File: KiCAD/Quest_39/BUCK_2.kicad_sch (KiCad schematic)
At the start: 33 parts, among them U12 AD626ANZ, U13 INA226, U14 LTM4611EV-PBF, U15 MCP4151-502E/SN

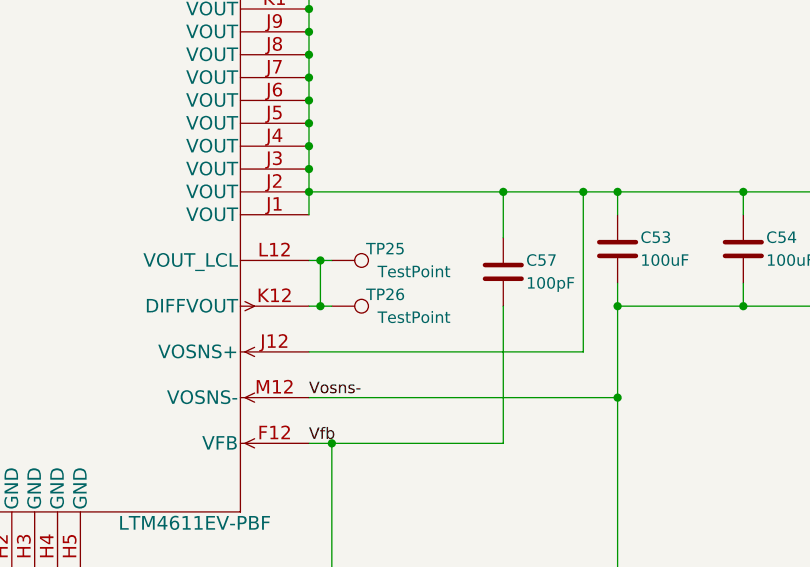
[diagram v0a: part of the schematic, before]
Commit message: Added 3rd buck converter section
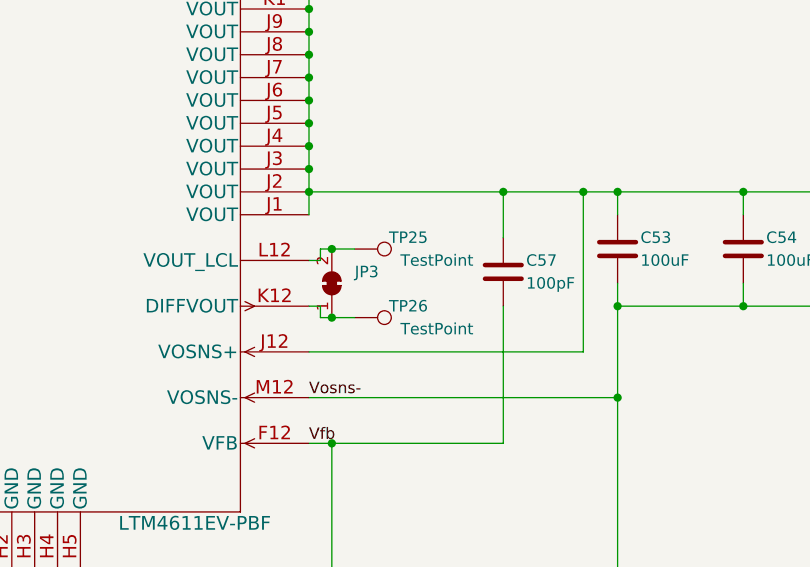
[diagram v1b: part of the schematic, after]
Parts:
- added JP3: SolderJumper_2_Bridged, Jumper:SolderJumper-2_P1.3mm_Bridged_RoundedPad1.0x1.5mm, symbol Jumper:SolderJumper_2_Bridged
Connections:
- net at TP25.1, U14.L12 (VOUT_LCL): now also JP3.2 (B); no longer TP26.1, U14.K12 (DIFFVOUT)
- new net: JP3.1 (A), TP26.1, U14.K12 (DIFFVOUT)
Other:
- moved on the sheet: TP25, TP26
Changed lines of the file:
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@@
   (junction (at 210.82 34.29) (diameter 0) (color 0 0 0 0)
   )
+  (junction (at 325.12 170.18) (diameter 0) (color 0 0 0 0)
+  )
   (junction (at 322.58 148.59) (diameter 0) (color 0 0 0 0)
   )
@@
   (junction (at 198.12 34.29) (diameter 0) (color 0 0 0 0)
   )
+  (junction (at 325.12 162.56) (diameter 0) (color 0 0 0 0)
+  )
   (junction (at 322.58 105.41) (diameter 0) (color 0 0 0 0)
   )
@@
   (junction (at 370.84 156.21) (diameter 0) (color 0 0 0 0)
   )
-  (junction (at 323.85 168.91) (diameter 0) (color 0 0 0 0)
-  )
   (junction (at 203.2 34.29) (diameter 0) (color 0 0 0 0)
   )
@@
   )
   (junction (at 370.84 168.91) (diameter 0) (color 0 0 0 0)
-  )
-  (junction (at 323.85 163.83) (diameter 0) (color 0 0 0 0)
   )
   (junction (at 91.44 34.29) (diameter 0) (color 0 0 0 0)
@@
     (stroke (width 0) (type default) (color 0 0 0 0))
   )
-  (wire (pts (xy 325.12 168.91) (xy 323.85 168.91))
-    (stroke (width 0) (type default) (color 0 0 0 0))
-  )
   (wire (pts (xy 322.58 140.97) (xy 322.58 143.51))
     (stroke (width 0) (type default) (color 0 0 0 0))
@@
     (stroke (width 0) (type default) (color 0 0 0 0))
   )
-  (wire (pts (xy 323.85 168.91) (xy 322.58 168.91))
-    (stroke (width 0) (type default) (color 0 0 0 0))
-  )
   (wire (pts (xy 322.58 62.23) (xy 322.58 64.77))
     (stroke (width 0) (type default) (color 0 0 0 0))
@@
     (stroke (width 0) (type default) (color 0 0 0 0))
   )
+  (wire (pts (xy 325.12 170.18) (xy 327.66 170.18))
+    (stroke (width 0) (type default) (color 0 0 0 0))
+  )
   (wire (pts (xy 208.28 34.29) (xy 210.82 34.29))
     (stroke (width 0) (type default) (color 0 0 0 0))
@@
     (stroke (width 0) (type default) (color 0 0 0 0))
   )
+  (wire (pts (xy 322.58 163.83) (xy 323.85 163.83))
+    (stroke (width 0) (type default) (color 0 0 0 0))
+  )
   (polyline (pts (xy 351.79 203.2) (xy 351.79 233.68))
     (stroke (width 0) (type default) (color 0 0 0 0))
@@
     (stroke (width 0) (type default) (color 0 0 0 0))
   )
-  (wire (pts (xy 323.85 163.83) (xy 323.85 168.91))
-    (stroke (width 0) (type default) (color 0 0 0 0))
-  )
   (wire (pts (xy 322.58 69.85) (xy 322.58 72.39))
     (stroke (width 0) (type default) (color 0 0 0 0))
@@
     (stroke (width 0) (type default) (color 0 0 0 0))
   )
+  (wire (pts (xy 322.58 168.91) (xy 323.85 168.91))
+    (stroke (width 0) (type default) (color 0 0 0 0))
+  )
   (wire (pts (xy 91.44 34.29) (xy 105.41 34.29))
     (stroke (width 0) (type default) (color 0 0 0 0))
@@
     (stroke (width 0) (type default) (color 0 0 0 0))
   )
+  (wire (pts (xy 323.85 170.18) (xy 325.12 170.18))
+    (stroke (width 0) (type default) (color 0 0 0 0))
+  )
   (wire (pts (xy 20.32 63.5) (xy 25.4 63.5))
     (stroke (width 0) (type default) (color 0 0 0 0))
@@
     (stroke (width 0) (type default) (color 0 0 0 0))
   )
+  (wire (pts (xy 325.12 162.56) (xy 327.66 162.56))
+    (stroke (width 0) (type default) (color 0 0 0 0))
+  )
   (wire (pts (xy 95.25 115.57) (xy 105.41 115.57))
     (stroke (width 0) (type default) (color 0 0 0 0))
@@
     (stroke (width 0) (type default) (color 0 0 0 0))
   )
-  (wire (pts (xy 323.85 163.83) (xy 325.12 163.83))
-    (stroke (width 0) (type default) (color 0 0 0 0))
-  )
   (wire (pts (xy 175.26 34.29) (xy 177.8 34.29))
     (stroke (width 0) (type default) (color 0 0 0 0))
@@
     (stroke (width 0) (type default) (color 0 0 0 0))
   )
-  (wire (pts (xy 322.58 163.83) (xy 323.85 163.83))
-    (stroke (width 0) (type default) (color 0 0 0 0))
-  )
   (wire (pts (xy 198.12 34.29) (xy 198.12 39.37))
     (stroke (width 0) (type default) (color 0 0 0 0))
@@
     (stroke (width 0) (type default) (color 0 0 0 0))
   )
+  (wire (pts (xy 323.85 163.83) (xy 323.85 162.56))
+    (stroke (width 0) (type default) (color 0 0 0 0))
+  )
   (polyline (pts (xy 13.97 26.67) (xy 87.63 26.67))
     (stroke (width 0) (type default) (color 0 0 0 0))
@@
     (stroke (width 0) (type default) (color 0 0 0 0))
   )
+  (wire (pts (xy 323.85 162.56) (xy 325.12 162.56))
+    (stroke (width 0) (type default) (color 0 0 0 0))
+  )
   (wire (pts (xy 370.84 156.21) (xy 370.84 158.75))
+    (stroke (width 0) (type default) (color 0 0 0 0))
+  )
+  (wire (pts (xy 323.85 168.91) (xy 323.85 170.18))
     (stroke (width 0) (type default) (color 0 0 0 0))
   )
@@
     (pin "2")
   )
-  (symbol (lib_id "Connector:TestPoint") (at 325.12 163.83 270) (unit 1)
-    (in_bom yes) (on_board yes)
-    (property "Reference" "TP25" (id 0) (at 328.93 162.56 90)
-      (effects (font (size 1.27 1.27)) (justify left))
-    )
-    (property "Value" "TestPoint" (id 1) (at 330.2 165.1 90)
-      (effects (font (size 1.27 1.27)) (justify left))
-    )
-    (property "Footprint" "TestPoint:TestPoint_Pad_D2.0mm" (id 2) (at 325.12 168.91 0)
-      (effects (font (size 1.27 1.27)) hide)
-    )
-    (property "Datasheet" "~" (id 3) (at 325.12 168.91 0)
+  (symbol (lib_id "Connector:TestPoint") (at 327.66 162.56 270) (unit 1)
+    (in_bom yes) (on_board yes)
+    (property "Reference" "TP25" (id 0) (at 331.47 161.29 90)
+      (effects (font (size 1.27 1.27)) (justify left))
+    )
+    (property "Value" "TestPoint" (id 1) (at 332.74 163.83 90)
+      (effects (font (size 1.27 1.27)) (justify left))
+    )
+    (property "Footprint" "TestPoint:TestPoint_Pad_D2.0mm" (id 2) (at 327.66 167.64 0)
+      (effects (font (size 1.27 1.27)) hide)
+    )
+    (property "Datasheet" "~" (id 3) (at 327.66 167.64 0)
       (effects (font (size 1.27 1.27)) hide)
     )
@@
     (pin "2")
   )
-  (symbol (lib_id "Connector:TestPoint") (at 325.12 168.91 270) (unit 1)
-    (in_bom yes) (on_board yes)
-    (property "Reference" "TP26" (id 0) (at 328.93 167.64 90)
-      (effects (font (size 1.27 1.27)) (justify left))
-    )
-    (property "Value" "TestPoint" (id 1) (at 330.2 170.18 90)
-      (effects (font (size 1.27 1.27)) (justify left))
-    )
-    (property "Footprint" "TestPoint:TestPoint_Pad_D2.0mm" (id 2) (at 325.12 173.99 0)
-      (effects (font (size 1.27 1.27)) hide)
-    )
-    (property "Datasheet" "~" (id 3) (at 325.12 173.99 0)
+  (symbol (lib_id "Connector:TestPoint") (at 327.66 170.18 270) (unit 1)
+    (in_bom yes) (on_board yes)
+    (property "Reference" "TP26" (id 0) (at 331.47 168.91 90)
+      (effects (font (size 1.27 1.27)) (justify left))
+    )
+    (property "Value" "TestPoint" (id 1) (at 332.74 171.45 90)
+      (effects (font (size 1.27 1.27)) (justify left))
+    )
+    (property "Footprint" "TestPoint:TestPoint_Pad_D2.0mm" (id 2) (at 327.66 175.26 0)
+      (effects (font (size 1.27 1.27)) hide)
+    )
+    (property "Datasheet" "~" (id 3) (at 327.66 175.26 0)
       (effects (font (size 1.27 1.27)) hide)
     )
@@
       (effects (font (size 1.27 1.27)) hide)
     )
+    (pin "1")
+    (pin "2")
+  )
+  (symbol (lib_id "Jumper:SolderJumper_2_Bridged") (at 325.12 166.37 90) (unit 1)
+    (in_bom yes) (on_board yes) (fields_autoplaced)
+    (property "Reference" "JP3" (id 0) (at 327.66 165.0999 90)
+      (effects (font (size 1.27 1.27)) (justify right))
+    )
+    (property "Value" "SolderJumper_2_Bridged" (id 1) (at 327.66 167.6399 90)
+      (effects (font (size 1.27 1.27)) (justify right) hide)
+    )
+    (property "Footprint" "Jumper:SolderJumper-2_P1.3mm_Bridged_RoundedPad1.0x1.5mm" (id 2) (at 325.12 166.37 0)
+      (effects (font (size 1.27 1.27)) hide)
+    )
+    (property "Datasheet" "~" (id 3) (at 325.12 166.37 0)
+      (effects (font (size 1.27 1.27)) hide)
+    )

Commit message: Added all the SolidWorks files, edited README
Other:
- title: (none) -> BUCK_2
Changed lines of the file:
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@@
 (kicad_sch (version 20211123) (generator eeschema)
   (paper "A3")
+  (title_block
+    (title "BUCK_2")
+    (date "2023-01-31")
+    (rev "1.0")
+  )
   (junction (at 200.66 34.29) (diameter 0) (color 0 0 0 0)
   )
